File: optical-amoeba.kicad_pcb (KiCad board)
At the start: 2 copper layers, 19.1 x 19 mm, 5 parts, among them J1 Conn_01x08_Male, Q1 Q_Photo_NPN_CE

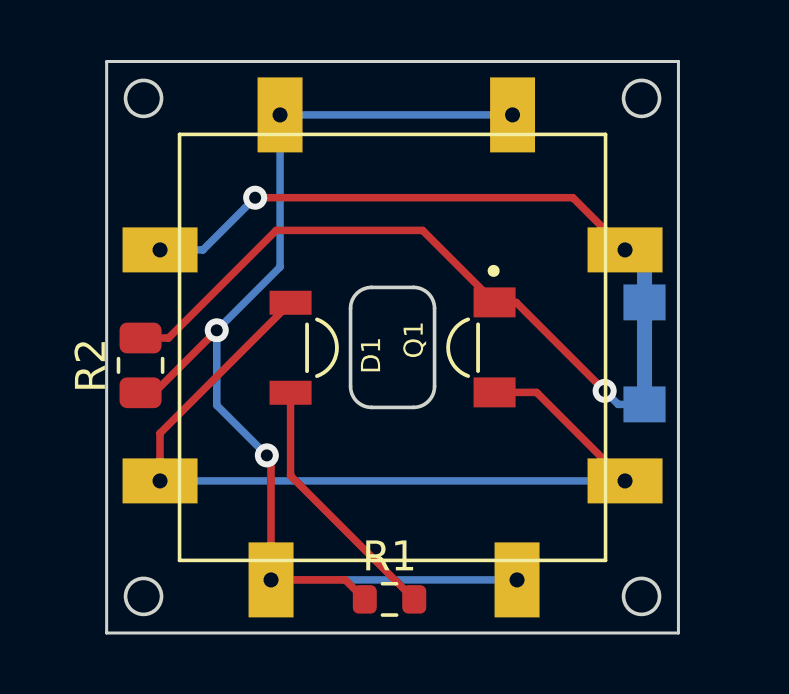
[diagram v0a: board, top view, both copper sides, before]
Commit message: Added PCB for full keyboard
 M .gitignore
A  OpticalSymbols_Library.kicad_sym
A  Optical_Parts.pretty/BlackPill_STLINK.kicad_mod
M  Optical_Parts.pretty/Everlight_IR_IR12-21C_TR8.kicad_mod
M  Optical_Parts.pretty/Everlight_PT_PT12-21C_TR8.kicad_mod
M  Optical_Parts.pretty/Gateron_Optical_Switch.kicad_mod
A  Optical_Parts.pretty/Gateron_Switch_Basic.kicad_mod
A  Optical_Parts.pretty/Switch_Cutout.kicad_mod
A  Optical_Parts.pretty/Switch_Cutout_1.25u.kicad_mod
A  Optical_Parts.pretty/Switch_Cutout_1.5u.kicad_mod
A  Optical_Parts.pretty/Switch_Cutout_1.75u.kicad_mod
M  README.md
A  keyboard-pcb/.gitignore
A  keyboard-pcb/fp-lib-table
A  keyboard-pcb/keyboard-pcb.kicad_pcb
A  keyboard-pcb/keyboard-pcb.kicad_prl
A  keyboard-pcb/keyboard-pcb.kicad_pro
A  keyboard-pcb/keyboard-pcb.kicad_sch
A  keyboard-pcb/placefp.py
A  keyboard-pcb/switch.kicad_sch
A  keyboard-pcb/sym-lib-table
M  optical-amoeba.kicad_pcb
M  optical-amoeba.kicad_sch
A  switch-cutout/.gitignore
A  switch-cutout/fp-lib-table
A  switch-cutout/switch-cutout.kicad_pcb
A  switch-cutout/switch-cutout.kicad_prl
A  switch-cutout/switch-cutout.kicad_pro
A  switch-cutout/switch-cutout.kicad_sch
A  sym-lib-table
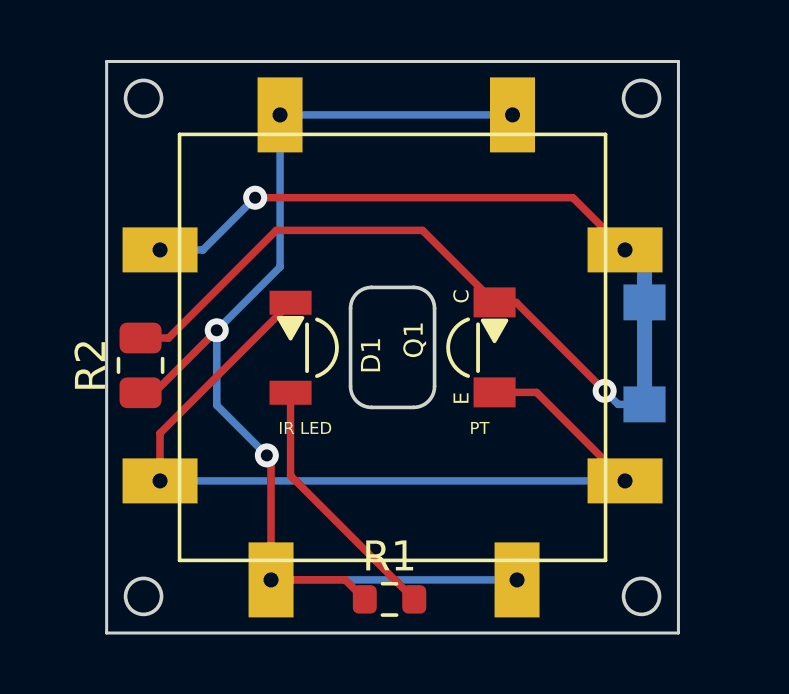
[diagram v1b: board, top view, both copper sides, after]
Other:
- board text added: "IR LED"
- board text added: "PT"

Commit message: Added footprints
M  Optical_Parts.pretty/BlackPill_STLINK.kicad_mod
M  Optical_Parts.pretty/BlackPill_STLINK2.kicad_mod
M  Optical_Parts.pretty/Everlight_IR_IR12-21C_TR8.kicad_mod
M  Optical_Parts.pretty/Everlight_PT_PT12-21C_TR8.kicad_mod
M  Optical_Parts.pretty/Gateron_Optical_Switch.kicad_mod
M  Optical_Parts.pretty/MountingHole_2.2mm_M2_jlcpcb.kicad_mod
M  Optical_Parts.pretty/Switch_Cutout.kicad_mod
M  Optical_Parts.pretty/Switch_Cutout_1.25u.kicad_mod
M  Optical_Parts.pretty/Switch_Cutout_1.5u.kicad_mod
M  Optical_Parts.pretty/Switch_Cutout_1.75u.kicad_mod
M  README.md
M  optical-amoeba.kicad_pcb
M  optical-amoeba.kicad_prl
M  optical-amoeba.kicad_sch
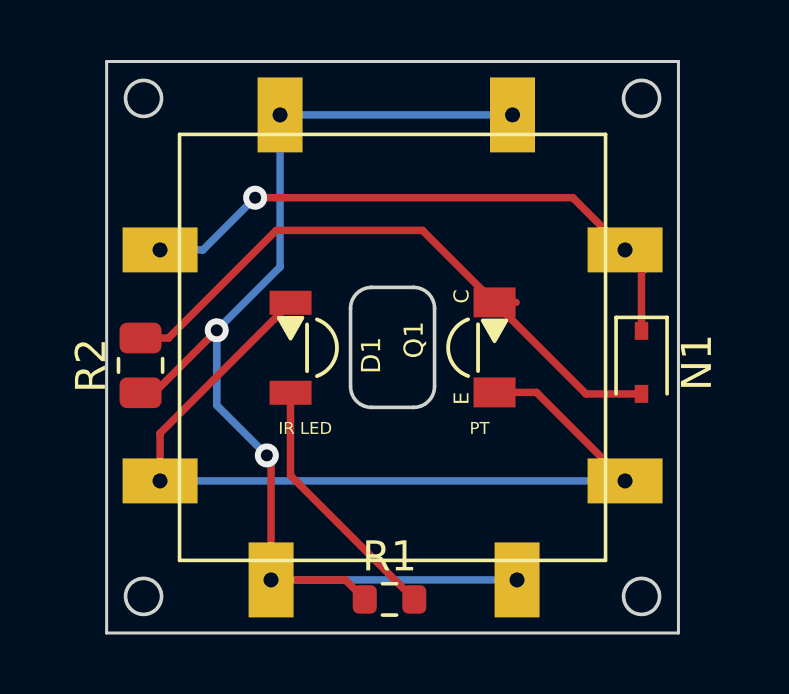
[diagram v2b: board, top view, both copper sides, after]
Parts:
- added N1: Diode1N4148WSSod323, Diode_SMD:D_SOD-323, F.Cu at (108.3, 100.5)
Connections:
- Q1 pad 1: Net-(J1-Pad2) -> Net-(N1-Pad2)
- R2 pad 2: Net-(J1-Pad2) -> Net-(N1-Pad2)
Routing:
- net Net-(N1-Pad2): track 0.00 -> 21.2 mm
- net Net-(J1-Pad2): track 39.6 -> 20.8 mm, vias 2 -> 1

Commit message: Separated power sourcde for PT and Led
Having same power source necessiates a diode; Diode degrades
performance at read pin

M  OpticalSymbols_Library.kicad_sym
M  Optical_Parts.pretty/Gateron_Optical_Switch.kicad_mod
M  optical-amoeba.kicad_pcb
M  optical-amoeba.kicad_prl
M  optical-amoeba.kicad_sch
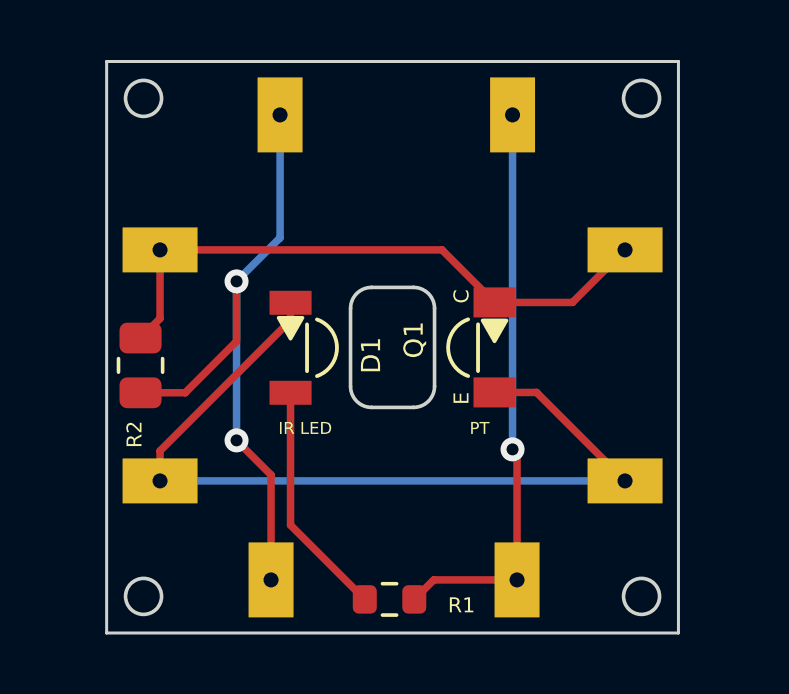
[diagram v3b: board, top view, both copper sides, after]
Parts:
- removed N1: Diode1N4148WSSod323, Diode_SMD:D_SOD-323
- turned R1 to 180 degrees
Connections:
- J1 pad 6: Net-(J1-Pad5) -> Net-(J1-Pad6)
- J1 pad 8: Net-(J1-Pad5) -> Net-(J1-Pad6)
- Q1 pad 1: Net-(N1-Pad2) -> Net-(J1-Pad2)
- R2 pad 1: Net-(J1-Pad5) -> Net-(J1-Pad6)
- R2 pad 2: Net-(N1-Pad2) -> Net-(J1-Pad2)
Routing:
- net Net-(J1-Pad6): track 0.00 -> 22.5 mm, vias 0 -> 2
- net Net-(N1-Pad2): track 21.2 -> 0.00 mm
- net Net-(J1-Pad5): track 39.9 -> 19.3 mm, vias 2 -> 1
- net Net-(D1-Pad2): track 8.60 -> 7.91 mm
- net Net-(J1-Pad2): track 20.8 -> 20.2 mm, vias 1 -> 0
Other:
- board text added: "3v3/5v"
- board text added: "Col"
- board text added: "Gnd"
- board text added: "Row"

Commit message: Add jlcpcb gerber and assembly files
M  OpticalSymbols_Library.kicad_sym
A  jlcpcb/gerber/optical-amoeba-B_Cu.gbl
A  jlcpcb/gerber/optical-amoeba-B_Mask.gbs
A  jlcpcb/gerber/optical-amoeba-B_Paste.gbp
A  jlcpcb/gerber/optical-amoeba-B_Silkscreen.gbo
A  jlcpcb/gerber/optical-amoeba-Edge_Cuts.gm1
A  jlcpcb/gerber/optical-amoeba-F_Cu.gtl
A  jlcpcb/gerber/optical-amoeba-F_Mask.gts
A  jlcpcb/gerber/optical-amoeba-F_Paste.gtp
A  jlcpcb/gerber/optical-amoeba-F_Silkscreen.gto
A  jlcpcb/gerber/optical-amoeba-NPTH-drl_map.gbr
A  jlcpcb/gerber/optical-amoeba-NPTH.drl
A  jlcpcb/gerber/optical-amoeba-PTH-drl_map.gbr
A  jlcpcb/gerber/optical-amoeba-PTH.drl
M  optical-amoeba.kicad_pcb
M  optical-amoeba.kicad_prl
M  optical-amoeba.kicad_sch
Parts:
- removed R1: R, Resistor_SMD:R_0603_1608Metric
- removed R2: R, Resistor_SMD:R_0805_2012Metric
- added RL1: R_Led, Resistor_SMD:R_0603_1608Metric, F.Cu at (99.9, 108.3)
- added RP1: R_PT, Resistor_SMD:R_0805_2012Metric, F.Cu at (91.8, 100.7)
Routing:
- net Net-(J1-Pad6): track 22.5 -> 21.8 mm
